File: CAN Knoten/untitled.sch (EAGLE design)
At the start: 7 parts, among them Q1 HC49-U

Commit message: 
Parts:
- added C4, C5: 100nF, rcl:C-EUC1206
- added C6, C7: 22pF, rcl:C-EUC1206
- added D1: (no value), AVR - XMEGA:ATXMEGA16D4/32D4/64D4/128D4-A
- added J1: (no value), InputOutputIO (rev18b):615004143821
- added JP1: (no value), jumper:JP2E
- added LED10, LED11, LED2, LED3, LED4, LED5, LED6, LED7, LED8, LED9: (no value), led:LEDSML1206
- added Q2: HC49-U - xMHz, Quarz - HC49UP:HC49-U
- added R10, R12, R13, R2, R3, R4, R5, R6, R7, R9: 560R, rcl:R-EU_R1206
- added R11, R8: 10k, rcl:R-EU_R1206
- added R14: 120R, rcl:R-EU_R1206
- added U$2: MCP2551-E/SN, Microchip_By_element14_Batch_1:MCP2551-E/SN
- C2, C3: value 100nF -> 22pF
- Q1: value HC49-U -> HC49-U - 16MHz
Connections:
- removed net MCP2515_MISO: U$1.SO
- new net DEBUG_RXD: D1.(RXD0/OC0C)PD2, J1.1
- new net DEBUG_TXD: D1.(TXD0/OC0D)PD3, J1.2
- new net MCP2515_RX0BF: LED2.C, U$1.~RX0BF
- new net MCP2515_RX1BF: LED3.C, U$1.~RX1BF
- new net MCP2515_TX0RTS: LED5.C, U$1.~TX0RTS
- new net MCP2515_TX1RTS: LED6.C, U$1.~TX1RTS
- new net MCP2515_TX2RTS: LED7.C, U$1.~TX2RTS
- new net MCP2551_CANH: JP1.1, U$2.CANH
- new net MCP2551_CANL: R14.1, U$2.CANL
- new net MCP2551_RS: R11.1, U$2.RS
- new net MCP2551_VREF: U$2.VREF
- new net N$1: LED2.A, R2.1
- new net N$10: LED11.A, R13.1
- new net N$11: LED10.A, R12.1
- new net N$12: JP1.2, R14.2
- new net N$15: C6.1, D1.PR0(XTAL2/TOSC2), Q2.2
- new net N$16: C7.1, D1.PR1(XTAL1/TOSC1), Q2.1
- new net N$17: C6.2, C7.2
- new net N$20: D1.(SDA/OC0A)PE0
- new net N$21: D1.(SCL/OC0B)PE1
- new net N$3: LED3.A, R3.1
- new net N$4: LED4.A, R4.1
- new net SPI_MISO: D1.(MISO)PD6, U$1.SO
- new net SPI_SLAVE_SELECT_HW: D1.(!SS!)PD4
- net GND: now also C4.1, C5.2, D1.GND@18, D1.GND@30, D1.GND@38, D1.GND@8, J1.3, U$2.VSS
- net MCP2515_INT: now also LED10.C
- net MCP2515_OSC2: now also LED11.C
- net MCP2515_RESET: now also R8.1
- net MCP2515_RXCAN: now also LED4.C, LED9.C, U$2.RXD
- net MCP2515_TXCAN: now also LED8.C, U$2.TXD
- net N$5: now also LED5.A, R5.1; no longer U$1.~RX0BF
- net N$6: now also LED6.A, R6.1; no longer U$1.~RX1BF
- net N$7: now also LED7.A, R7.1; no longer U$1.~TX0RTS
- net N$8: now also LED8.A, R9.1; no longer U$1.~TX1RTS
- net N$9: now also LED9.A, R10.1; no longer U$1.~TX2RTS
- net SPI_MOSI: now also D1.(MOSI)PD5
- net SPI_SCK: now also D1.(EVOUT/CLKOUT/SCK)PD7
- net VCC: now also C4.2, C5.1, D1.AVCC, D1.VCC@19, D1.VCC@31, D1.VCC@9, J1.4, R10.2, R11.2, R12.2, R13.2, R2.2, R3.2, R4.2, R5.2, R6.2, R7.2, R8.2, R9.2, U$2.VDD
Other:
- note added: "Stellung | Mode ---------------------------------- 1 + 2 | Termination an 2 + 3 | Termination aus"
- moved on the sheet: C1, C2, C3, LED1, Q1, R1

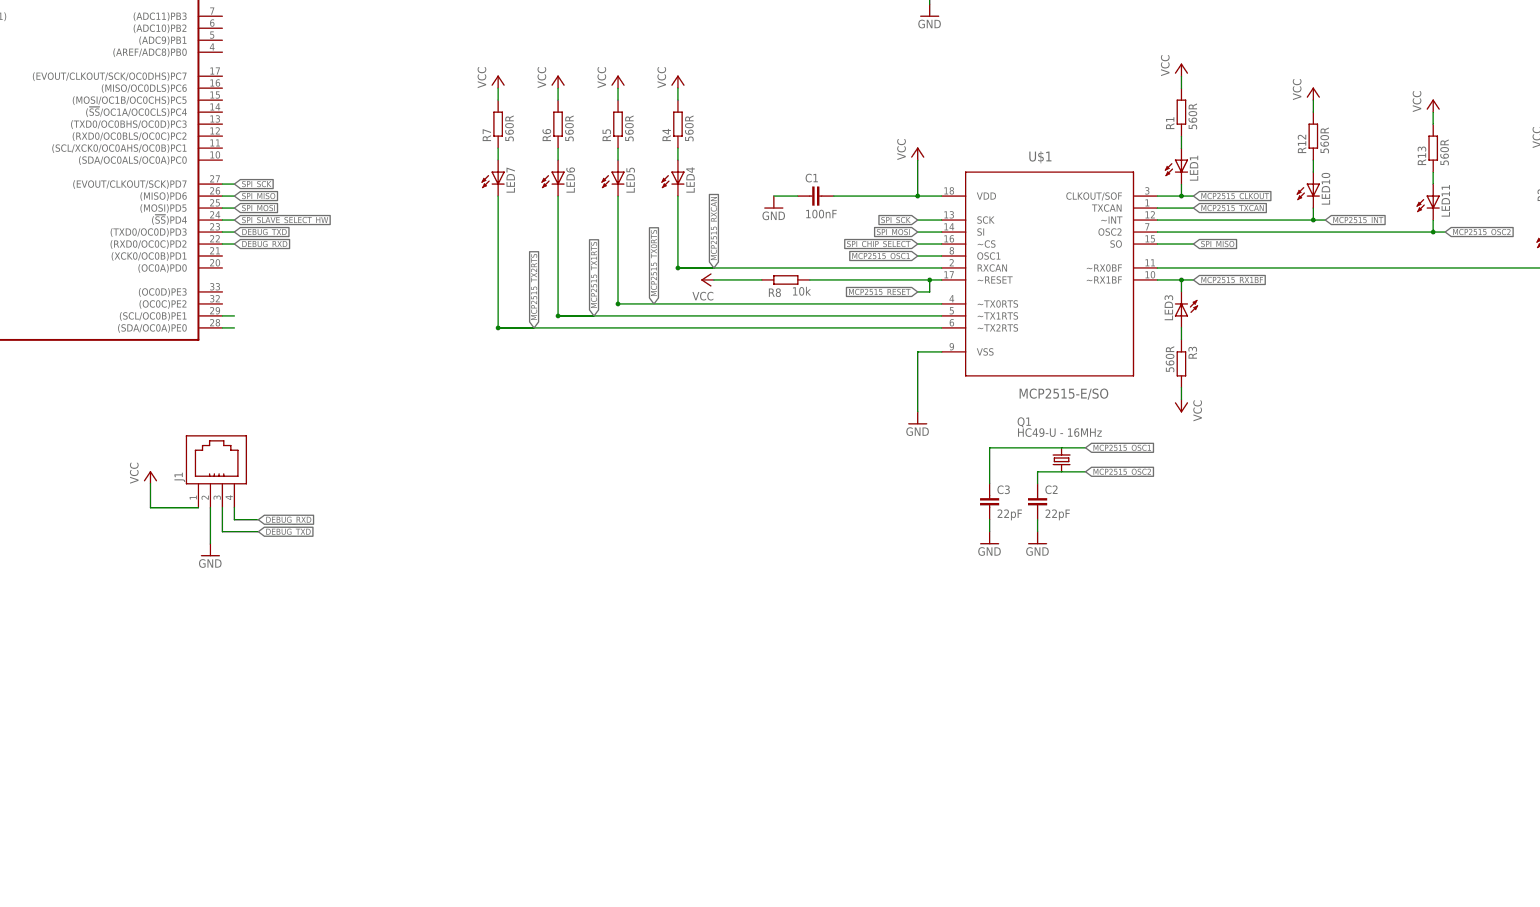
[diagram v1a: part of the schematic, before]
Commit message: 
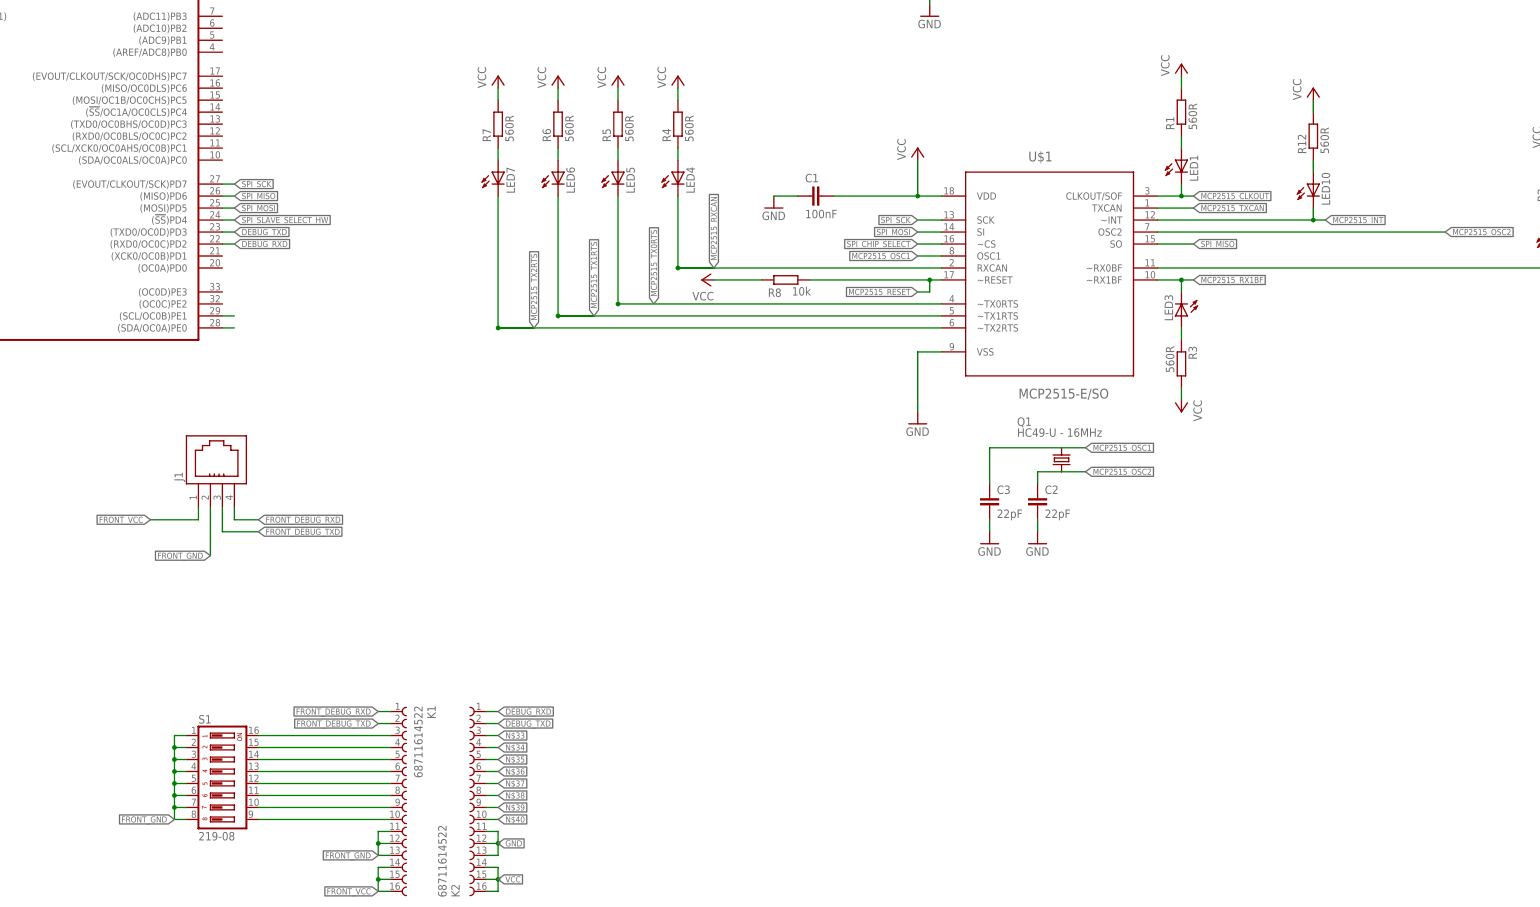
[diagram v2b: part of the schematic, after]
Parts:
- removed LED11: (no value), led:LEDSML1206
- removed R13: 560R, rcl:R-EU_R1206
- added K1, K2: 68711614522, Wurth_FPC_FFC:68711614522
- added S1: 219-08, switch-dil:219-08
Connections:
- removed net N$10: LED11.A, R13.1
- new net FRONT_DEBUG_RXD: J1.1, K1.1
- new net FRONT_DEBUG_TXD: J1.2, K1.2
- new net FRONT_GND: J1.3, K1.11, K1.12, K1.13, S1.1, S1.2, S1.3, S1.4, S1.5, S1.6, S1.7, S1.8
- new net FRONT_VCC: J1.4, K1.14, K1.15, K1.16
- new net N$22: K1.3, S1.16
- new net N$23: K1.4, S1.15
- new net N$24: K1.5, S1.14
- new net N$25: K1.6, S1.13
- new net N$26: K1.7, S1.12
- new net N$27: K1.8, S1.11
- new net N$28: K1.9, S1.10
- new net N$29: K1.10, S1.9
- new net N$33: K2.3
- new net N$34: K2.4
- new net N$35: K2.5
- new net N$36: K2.6
- new net N$37: K2.7
- new net N$38: K2.8
- new net N$39: K2.9
- new net N$40: K2.10
- net DEBUG_RXD: now also K2.1; no longer J1.1
- net DEBUG_TXD: now also K2.2; no longer J1.2
- net GND: now also K2.11, K2.12, K2.13; no longer J1.3
- net MCP2515_OSC2: no longer LED11.C
- net VCC: now also K2.14, K2.15, K2.16; no longer J1.4, R13.2

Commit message: 
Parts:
- removed LED4, LED5, LED6, LED7, LED8, LED9: (no value), led:LEDSML1206
- removed R10, R4, R5, R6, R7, R9: 560R, rcl:R-EU_R1206
- added IC1, IC2: 74LS165D, 74xx-us:74LS165D
- added K3, K4: 68711614522, Wurth_FPC_FFC:68711614522
- added RN1, RN3: (no value), resistor-array:745-10
- added S2: 219-08, switch-dil:219-08
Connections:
- removed net N$33: K2.3
- removed net N$34: K2.4
- removed net N$35: K2.5
- removed net N$36: K2.6
- removed net N$37: K2.7
- removed net N$38: K2.8
- removed net N$39: K2.9
- removed net N$40: K2.10
- new net 74XX165_CLK: D1.(AREF/ADC8)PB0, IC1A.CLK, IC2A.CLK
- new net 74XX165_OUT: D1.(ADC11)PB3, IC2A.QH
- new net 74XX165_SH/LD_IC1: D1.(ADC9)PB1, IC1A.SH/!LD
- new net 74XX165_SH/LD_IC2: D1.(ADC10)PB2, IC2A.SH/!LD
- new net CAN_BITRATE_0: IC2A.A, K4.3
- new net CAN_BITRATE_1: IC2A.B, K4.4
- new net CAN_BITRATE_2: IC2A.C, K4.5
- new net CAN_BITRATE_3: IC2A.D, K4.6
- new net CAN_BITRATE_4: IC2A.E, K4.7
- new net CAN_BITRATE_5: IC2A.F, K4.8
- new net CAN_BITRATE_6: IC2A.G, K4.9
- new net CAN_BITRATE_7: IC2A.H, K4.10
- new net N$13: D1.(AREF/AC0/ADC0)PA0
- new net N$14: D1.(AC1/ADC1)PA1
- new net N$18: D1.(AC2/ADC2)PA2
- new net N$19: K3.9, RN1.8, S2.10
- new net N$2: IC1A.QH, IC2A.SER
- new net N$30: K3.10, RN1.9, S2.9
- new net N$31: D1.(XCK0/OC0B)PD1
- new net NODE_ID_0: IC1A.A, K2.3
- new net NODE_ID_1: IC1A.B, K2.4
- new net NODE_ID_2: IC1A.C, K2.5
- new net NODE_ID_3: IC1A.D, K2.6
- new net NODE_ID_4: IC1A.E, K2.7
- new net NODE_ID_5: IC1A.F, K2.8
- new net NODE_ID_6: IC1A.G, K2.9
- new net NODE_ID_7: IC1A.H, K2.10
- new net REAR_GND: K3.14, K3.15, K3.16, S2.1, S2.2, S2.3, S2.4, S2.5, S2.6, S2.7, S2.8
- new net REAR_VCC: K3.1, K3.11, K3.12, K3.13, K3.2, RN1.10, RN1.5
- net FRONT_GND: now also K1.14, K1.15, K1.16; no longer K1.11, K1.12, K1.13
- net FRONT_VCC: now also K1.11, K1.12, K1.13, RN3.10, RN3.5; no longer K1.14, K1.15, K1.16
- net GND: now also IC1A.INH, IC1P.GND, IC2A.INH, IC2P.GND, K2.14, K2.15, K2.16, K4.14, K4.15, K4.16; no longer K2.11, K2.12, K2.13
- net MCP2515_CLKOUT: no longer LED1.C
- net MCP2515_INT: now also D1.(AC3/ADC3)PA3
- net MCP2515_RXCAN: now also D1.(AC4/ADC4)PA4; no longer LED4.C, LED9.C
- net MCP2515_TX0RTS: now also D1.(AC5/ADC5)PA5; no longer LED5.C
- net MCP2515_TX1RTS: now also D1.(AC6/ADC6)PA6; no longer LED6.C
- net MCP2515_TX2RTS: now also D1.(OUT/AC0/AC7/ADC7)PA7; no longer LED7.C
- net MCP2515_TXCAN: no longer LED8.C
- net N$22: now also RN3.1
- net N$23: now also RN3.2
- net N$24: now also RN3.3
- net N$25: now also RN3.4
- net N$26: now also RN3.6
- net N$27: now also RN3.7
- net N$28: now also RN3.8
- net N$29: now also RN3.9
- net N$4: now also K3.3, RN1.1, S2.16; no longer LED4.A, R4.1
- net N$5: now also K3.4, RN1.2, S2.15; no longer LED5.A, R5.1
- net N$6: now also K3.5, RN1.3, S2.14; no longer LED6.A, R6.1
- net N$7: now also K3.6, RN1.4, S2.13; no longer LED7.A, R7.1
- net N$8: now also K3.7, RN1.6, S2.12; no longer LED8.A, R9.1
- net N$9: now also K3.8, RN1.7, S2.11; no longer LED9.A, R10.1
- net SPI_SLAVE_SELECT_HW: now also LED1.C
- net VCC: now also IC1P.VCC, IC2P.VCC, K2.11, K2.12, K2.13, K4.1, K4.11, K4.12, K4.13, K4.2; no longer K2.14, K2.15, K2.16, R10.2, R4.2, R5.2, R6.2, R7.2, R9.2
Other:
- moved on the sheet: J1, K1, K2, LED1, LED2, R1, R11, R2, S1

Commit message: 
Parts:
- added LED4, LED5: (no value), led:LEDSML1206
- added R4, R5: 560R, rcl:R-EU_R1206
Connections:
- removed net N$31: D1.(XCK0/OC0B)PD1
- new net N$33: K3.1, LED5.C
- new net N$34: K3.2, LED4.C
- new net N$35: LED4.A, R4.1
- new net N$36: LED5.A, R5.1
- net MCP2515_RXCAN: now also K4.2
- net MCP2515_TXCAN: now also K4.1
- net REAR_VCC: now also R4.2, R5.2; no longer K3.1, K3.2
- net SPI_CHIP_SELECT: now also D1.(XCK0/OC0B)PD1
- net VCC: no longer K4.1, K4.2
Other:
- moved on the sheet: IC2, K3, K4, RN1, S2
